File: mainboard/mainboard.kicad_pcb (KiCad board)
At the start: 2 copper layers, 103 x 41 mm, 25 parts, among them P1 CONN_01X06, P2 CONN_01X08, P3 CONN_01X08, SW1 SW_PUSH, SW2 SW_PUSH, SW3 SW_PUSH, SW4 SW_PUSH, SW5 SW_PUSH, SW6 SW_PUSH, U1 LPC812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

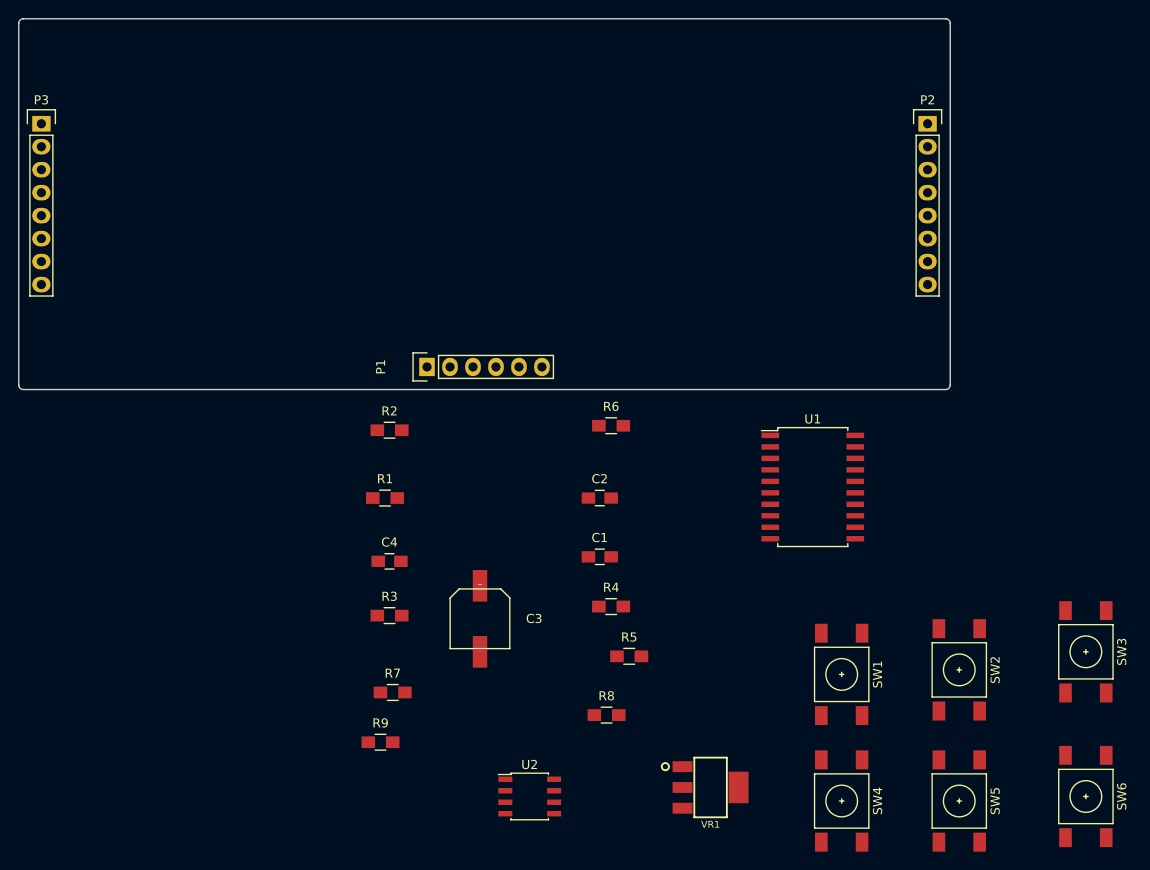
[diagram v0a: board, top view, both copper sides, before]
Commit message: Component placement on PCB.
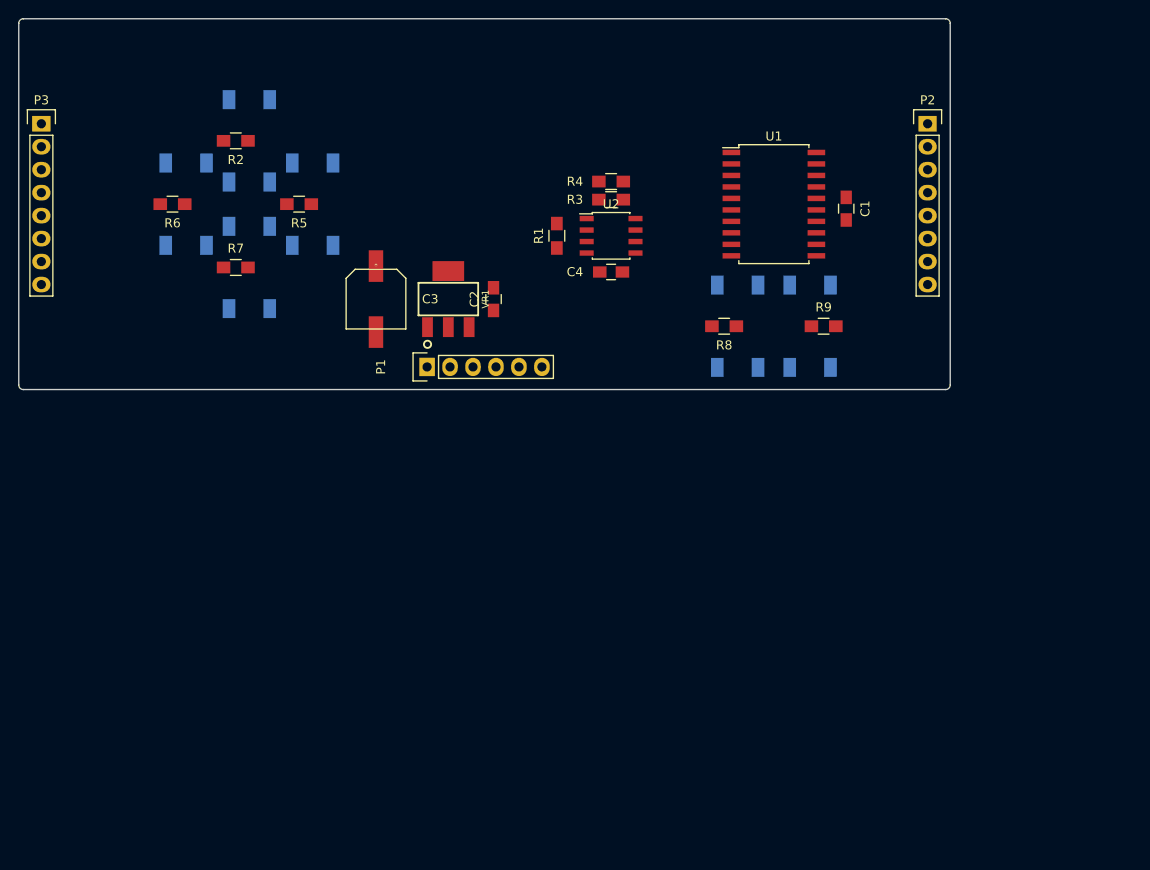
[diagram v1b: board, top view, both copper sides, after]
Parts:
- SW1, SW2, SW3, SW4, SW5, SW6: moved to B.Cu
- moved SW3 111.1 mm to (-33.0, 0.00)
- moved SW2 90.2 mm to (-26.0, 7.00)
- moved SW4 88.2 mm to (-19.0, 0.00)
- moved SW1 88.2 mm to (-26.0, -7.00)
- moved R9 67.2 mm to (37.5, 13.5)
- moved U2 62.6 mm to (14.0, 3.50)
- moved R5 61.9 mm to (-20.5, 0.00), turned to 180 degrees
- moved VR1 61.3 mm to (-4.00, 10.5), turned to 90 degrees
- moved SW6 60.3 mm to (36.0, 13.5), turned to 180 degrees
- moved SW5 57.9 mm to (28.0, 13.5)
- moved R6 54.3 mm to (-34.5, 0.00), turned to 180 degrees
- moved R3 52.1 mm to (14.0, -0.50)
- moved R7 50.1 mm to (-27.5, 7.00)
- moved C1 47.2 mm to (40.0, 0.50), turned to 270 degrees
- moved R4 47.0 mm to (14.0, -2.50)
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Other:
- board text added: "Mini Clock v0.1 By Martin Atkins https://github.com/apparentlymart/miniclock"

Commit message: DC regulator traces.
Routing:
- net GND: track 0.00 -> 19.7 mm
- net +5V: track 0.00 -> 8.72 mm
- net +3V3: track 0.00 -> 8.23 mm
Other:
- net class Default: trace_width 0.25 -> 0.2
- net class Power added: clearance 0.2, trace_width 0.4, via_dia 0.8, via_drill 0.4
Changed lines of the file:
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@@
     (thickness 1.6)
     (drawings 9)
-    (tracks 0)
+    (tracks 15)
     (zones 0)
     (modules 25)
@@
   )
   (setup
-    (last_trace_width 0.25)
+    (last_trace_width 0.2)
     (trace_clearance 0.2)
     (zone_clearance 0.508)
@@
   (net_class Default "This is the default net class."
     (clearance 0.2)
-    (trace_width 0.25)
+    (trace_width 0.2)
     (via_dia 0.6)
     (via_drill 0.4)
     (uvia_dia 0.3)
     (uvia_drill 0.1)
-    (add_net +3V3)
-    (add_net +5V)
     (add_net CTS)
-    (add_net GND)
     (add_net MISO)
     (add_net MOSI)
@@
     (add_net ~RIGHT)
     (add_net ~UP)
+  )
+  (net_class Power ""
+    (clearance 0.2)
+    (trace_width 0.4)
+    (via_dia 0.8)
+    (via_drill 0.4)
+    (uvia_dia 0.3)
+    (uvia_drill 0.1)
+    (add_net +3V3)
+    (add_net +5V)
+    (add_net GND)
   )
   (module Capacitors_SMD:C_0805_HandSoldering (layer F.Cu)
@@
   (gr_line (start -51 20.5) (end 51 20.5) (layer Edge.Cuts) (width 0.15))
   (gr_line (start -51.5 -20) (end -51.5 20) (layer Edge.Cuts) (width 0.15))
+  (segment (start -12 14.15) (end -6.85 14.15) (width 0.4) (layer F.Cu) (net 1))
+  (segment (start -6.85 14.15) (end -6.3 13.6) (width 0.4) (layer F.Cu) (net 1))
+  (segment (start 1 9.25) (end -2.45 9.25) (width 0.4) (layer F.Cu) (net 1))
+  (segment (start -2.45 9.25) (end -6.3 13.1) (width 0.4) (layer F.Cu) (net 1))
+  (segment (start -6.3 13.1) (end -6.3 13.6) (width 0.4) (layer F.Cu) (net 1))
+  (segment (start -6.35 18) (end -6.35 13.65) (width 0.4) (layer F.Cu) (net 1))
+  (segment (start -6.35 13.65) (end -6.3 13.6) (width 0.4) (layer F.Cu) (net 1))
+  (segment (start -12 6.85) (end -4.55 6.85) (width 0.4) (layer F.Cu) (net 2))
+  (segment (start -4.55 6.85) (end -4 7.4) (width 0.4) (layer F.Cu) (net 2))
+  (segment (start 1 11.75) (end 1 12.9) (width 0.4) (layer F.Cu) (net 3))
+  (segment (start 1 12.9) (end 0.3 13.6) (width 0.4) (layer F.Cu) (net 3))
+  (segment (start 0.3 13.6) (end -0.7 13.6) (width 0.4) (layer F.Cu) (net 3))
+  (segment (start -0.7 13.6) (end -1.7 13.6) (width 0.4) (layer F.Cu) (net 3))
+  (segment (start -1.7 13.6) (end -1.7 17.57) (width 0.4) (layer F.Cu) (net 3))
+  (segment (start -1.7 17.57) (end -1.27 18) (width 0.4) (layer F.Cu) (net 3))
 )

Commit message: Button traces.
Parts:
- moved R5 9.90 mm to (-27.5, 7.00)
- moved R7 9.90 mm to (-20.5, 0.00), turned to 180 degrees
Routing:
- net Net-(R9-Pad2): track 0.00 -> 11.1 mm, vias 0 -> 1
- net Net-(R8-Pad2): track 0.00 -> 11.1 mm, vias 0 -> 1
- net Net-(R2-Pad2): track 0.00 -> 11.1 mm, vias 0 -> 1
- net Net-(R7-Pad2): track 0.00 -> 11.1 mm, vias 0 -> 1
- net Net-(R6-Pad2): track 0.00 -> 11.1 mm, vias 0 -> 1
- net Net-(R5-Pad2): track 0.00 -> 11.1 mm, vias 0 -> 1
- net GND: track 19.7 -> 29.6 mm, vias 0 -> 6
- added copper zone on B.Cu, net GND
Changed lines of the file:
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@@
     (thickness 1.6)
     (drawings 9)
-    (tracks 15)
+    (tracks 63)
     (zones 0)
     (modules 25)
@@
   )
   (module Resistors_SMD:R_0805_HandSoldering (layer F.Cu)
-    (at -20.5 0 180)
+    (at -27.5 7 180)
     (descr "Resistor SMD 0805, hand soldering")
     (tags "resistor 0805")
@@
   )
   (module Resistors_SMD:R_0805_HandSoldering (layer F.Cu)
-    (at -27.5 7)
+    (at -20.5 0 180)
     (descr "Resistor SMD 0805, hand soldering")
     (tags "resistor 0805")
     (attr smd)
-    (fp_text reference R7 (at 0 -2.1) (layer F.SilkS)
-      (effects (font (size 1 1) (thickness 0.15)))
-    )
-    (fp_text value R (at 0 2.1) (layer F.Fab)
+    (fp_text reference R7 (at 0 -2.1 180) (layer F.SilkS)
+      (effects (font (size 1 1) (thickness 0.15)))
+    )
+    (fp_text value R (at 0 2.1 180) (layer F.Fab)
       (effects (font (size 1 1) (thickness 0.15)))
     )
@@
     (fp_line (start 0.6 0.875) (end -0.6 0.875) (layer F.SilkS) (width 0.15))
     (fp_line (start -0.6 -0.875) (end 0.6 -0.875) (layer F.SilkS) (width 0.15))
-    (pad 1 smd rect (at -1.35 0) (size 1.5 1.3) (layers F.Cu F.Paste F.Mask)
-      (net 1 GND))
-    (pad 2 smd rect (at 1.35 0) (size 1.5 1.3) (layers F.Cu F.Paste F.Mask)
+    (pad 1 smd rect (at -1.35 0 180) (size 1.5 1.3) (layers F.Cu F.Paste F.Mask)
+      (net 1 GND))
+    (pad 2 smd rect (at 1.35 0 180) (size 1.5 1.3) (layers F.Cu F.Paste F.Mask)
       (net 27 "Net-(R7-Pad2)"))
     (model Resistors_SMD.3dshapes/R_0805_HandSoldering.wrl
@@
   (gr_line (start -51 20.5) (end 51 20.5) (layer Edge.Cuts) (width 0.15))
   (gr_line (start -51.5 -20) (end -51.5 20) (layer Edge.Cuts) (width 0.15))
+  (segment (start 36.15 13.5) (end 34.5 13.5) (width 0.4) (layer F.Cu) (net 1))
+  (via (at 34.5 13.5) (size 0.8) (drill 0.4) (layers F.Cu B.Cu) (net 1))
+  (segment (start 27.85 13.5) (end 29.5 13.5) (width 0.4) (layer F.Cu) (net 1))
+  (via (at 29.5 13.5) (size 0.8) (drill 0.4) (layers F.Cu B.Cu) (net 1))
+  (segment (start -26.15 7) (end -24.5 7) (width 0.4) (layer F.Cu) (net 1))
+  (via (at -24.5 7) (size 0.8) (drill 0.4) (layers F.Cu B.Cu) (net 1))
+  (segment (start -26.15 -7) (end -24.5 -7) (width 0.4) (layer F.Cu) (net 1))
+  (via (at -24.5 -7) (size 0.8) (drill 0.4) (layers F.Cu B.Cu) (net 1))
+  (segment (start -33.15 0) (end -31.5 0) (width 0.4) (layer F.Cu) (net 1))
+  (via (at -31.5 0) (size 0.8) (drill 0.4) (layers F.Cu B.Cu) (net 1))
+  (segment (start -19.15 0) (end -17.5 0) (width 0.4) (layer F.Cu) (net 1))
+  (via (at -17.5 0) (size 0.8) (drill 0.4) (layers F.Cu B.Cu) (net 1))
   (segment (start -12 14.15) (end -6.85 14.15) (width 0.4) (layer F.Cu) (net 1))
   (segment (start -6.85 14.15) (end -6.3 13.6) (width 0.4) (layer F.Cu) (net 1))
@@
   (segment (start -1.7 13.6) (end -1.7 17.57) (width 0.4) (layer F.Cu) (net 3))
   (segment (start -1.7 17.57) (end -1.27 18) (width 0.4) (layer F.Cu) (net 3))
+  (segment (start -27.5 -7) (end -27.5 -3.2) (width 0.2) (layer B.Cu) (net 22))
+  (segment (start -27.5 -3.2) (end -28.25 -2.45) (width 0.2) (layer B.Cu) (net 22))
+  (segment (start -27.5 -7) (end -27.5 -10.8) (width 0.2) (layer B.Cu) (net 22))
+  (segment (start -27.5 -10.8) (end -28.25 -11.55) (width 0.2) (layer B.Cu) (net 22))
+  (segment (start -28.85 -7) (end -27.5 -7) (width 0.2) (layer F.Cu) (net 22))
+  (via (at -27.5 -7) (size 0.6) (drill 0.4) (layers F.Cu B.Cu) (net 22))
+  (segment (start -27.5 7) (end -27.5 10.8) (width 0.2) (layer B.Cu) (net 25))
+  (segment (start -27.5 10.8) (end -28.25 11.55) (width 0.2) (layer B.Cu) (net 25))
+  (segment (start -27.5 7) (end -27.5 3.2) (width 0.2) (layer B.Cu) (net 25))
+  (segment (start -27.5 3.2) (end -28.25 2.45) (width 0.2) (layer B.Cu) (net 25))
+  (segment (start -28.85 7) (end -27.5 7) (width 0.2) (layer F.Cu) (net 25))
+  (via (at -27.5 7) (size 0.6) (drill 0.4) (layers F.Cu B.Cu) (net 25))
+  (segment (start -34.5 0) (end -34.5 3.8) (width 0.2) (layer B.Cu) (net 26))
+  (segment (start -34.5 3.8) (end -35.25 4.55) (width 0.2) (layer B.Cu) (net 26))
+  (segment (start -34.5 0) (end -34.5 -3.8) (width 0.2) (layer B.Cu) (net 26))
+  (segment (start -34.5 -3.8) (end -35.25 -4.55) (width 0.2) (layer B.Cu) (net 26))
+  (segment (start -35.85 0) (end -34.5 0) (width 0.2) (layer F.Cu) (net 26))
+  (via (at -34.5 0) (size 0.6) (drill 0.4) (layers F.Cu B.Cu) (net 26))
+  (segment (start -20.5 0) (end -20.5 3.8) (width 0.2) (layer B.Cu) (net 27))
+  (segment (start -20.5 3.8) (end -21.25 4.55) (width 0.2) (layer B.Cu) (net 27))
+  (segment (start -20.5 0) (end -20.5 -3.8) (width 0.2) (layer B.Cu) (net 27))
+  (segment (start -20.5 -3.8) (end -21.25 -4.55) (width 0.2) (layer B.Cu) (net 27))
+  (segment (start -21.85 0) (end -20.5 0) (width 0.2) (layer F.Cu) (net 27))
+  (via (at -20.5 0) (size 0.6) (drill 0.4) (layers F.Cu B.Cu) (net 27))
+  (segment (start 26.5 13.5) (end 26.5 17.3) (width 0.2) (layer B.Cu) (net 28))
+  (segment (start 26.5 17.3) (end 25.75 18.05) (width 0.2) (layer B.Cu) (net 28))
+  (segment (start 26.5 13.5) (end 26.5 9.7) (width 0.2) (layer B.Cu) (net 28))
+  (segment (start 26.5 9.7) (end 25.75 8.95) (width 0.2) (layer B.Cu) (net 28))
+  (segment (start 25.15 13.5) (end 26.5 13.5) (width 0.2) (layer F.Cu) (net 28))
+  (via (at 26.5 13.5) (size 0.6) (drill 0.4) (layers F.Cu B.Cu) (net 28))
+  (segment (start 37.5 13.5) (end 37.5 17.3) (width 0.2) (layer B.Cu) (net 29))
+  (segment (start 37.5 17.3) (end 38.25 18.05) (width 0.2) (layer B.Cu) (net 29))
+  (segment (start 37.5 13.5) (end 37.5 9.7) (width 0.2) (layer B.Cu) (net 29))
+  (segment (start 37.5 9.7) (end 38.25 8.95) (width 0.2) (layer B.Cu) (net 29))
+  (segment (start 38.85 13.5) (end 37.5 13.5) (width 0.2) (layer F.Cu) (net 29))
+  (via (at 37.5 13.5) (size 0.6) (drill 0.4) (layers F.Cu B.Cu) (net 29))
+  (zone (net 1) (net_name GND) (layer B.Cu) (hatch edge 0.508)
+    (connect_pads (clearance 0.508))
+    (min_thickness 0.254)
+    (fill yes (arc_segments 16) (thermal_gap 0.508) (thermal_bridge_width 0.508))
+    (polygon
+      (pts
+        (xy -51 -20) (xy 51 -20) (xy 51 20) (xy -51 20)
+      )
+    )
+  )
 )

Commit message: RTC traces.
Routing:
- net +3V3: track 8.23 -> 23.2 mm
- net SDA: track 0.00 -> 7.15 mm
- net GND: track 29.6 -> 33.6 mm
- net SQW: track 0.00 -> 3.60 mm
- net SCL: track 0.00 -> 2.71 mm
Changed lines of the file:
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@@
     (thickness 1.6)
     (drawings 9)
-    (tracks 63)
+    (tracks 84)
     (zones 0)
     (modules 25)
@@
   (gr_line (start -51 20.5) (end 51 20.5) (layer Edge.Cuts) (width 0.15))
   (gr_line (start -51.5 -20) (end -51.5 20) (layer Edge.Cuts) (width 0.15))
+  (segment (start 16.7 4.135) (end 16.7 5.405) (width 0.4) (layer F.Cu) (net 1))
+  (segment (start 16.7 5.405) (end 16.7 6.05) (width 0.4) (layer F.Cu) (net 1))
+  (segment (start 16.7 6.05) (end 15.25 7.5) (width 0.4) (layer F.Cu) (net 1))
   (segment (start 36.15 13.5) (end 34.5 13.5) (width 0.4) (layer F.Cu) (net 1))
   (via (at 34.5 13.5) (size 0.8) (drill 0.4) (layers F.Cu B.Cu) (net 1))
@@
   (segment (start -6.35 18) (end -6.35 13.65) (width 0.4) (layer F.Cu) (net 1))
   (segment (start -6.35 13.65) (end -6.3 13.6) (width 0.4) (layer F.Cu) (net 1))
+  (segment (start 12.75 7.5) (end 12.75 3.14) (width 0.4) (layer F.Cu) (net 2))
+  (segment (start 12.75 3.14) (end 12.475 2.865) (width 0.4) (layer F.Cu) (net 2))
+  (segment (start 12.475 2.865) (end 11.3 2.865) (width 0.4) (layer F.Cu) (net 2))
+  (segment (start 12.65 -2.5) (end 12.65 -0.5) (width 0.4) (layer F.Cu) (net 2))
+  (segment (start 12.65 -0.5) (end 12.65 2.69) (width 0.4) (layer F.Cu) (net 2))
+  (segment (start 12.65 2.69) (end 12.475 2.865) (width 0.4) (layer F.Cu) (net 2))
+  (segment (start 11.3 2.865) (end 8.715 2.865) (width 0.4) (layer F.Cu) (net 2))
+  (segment (start 8.715 2.865) (end 8 2.15) (width 0.4) (layer F.Cu) (net 2))
   (segment (start -12 6.85) (end -4.55 6.85) (width 0.4) (layer F.Cu) (net 2))
   (segment (start -4.55 6.85) (end -4 7.4) (width 0.4) (layer F.Cu) (net 2))
@@
   (segment (start -1.7 13.6) (end -1.7 17.57) (width 0.4) (layer F.Cu) (net 3))
   (segment (start -1.7 17.57) (end -1.27 18) (width 0.4) (layer F.Cu) (net 3))
+  (segment (start 11.3 4.135) (end 8.715 4.135) (width 0.2) (layer F.Cu) (net 21))
+  (segment (start 8.715 4.135) (end 8 4.85) (width 0.2) (layer F.Cu) (net 21))
   (segment (start -27.5 -7) (end -27.5 -3.2) (width 0.2) (layer B.Cu) (net 22))
   (segment (start -27.5 -3.2) (end -28.25 -2.45) (width 0.2) (layer B.Cu) (net 22))
@@
   (segment (start -28.85 -7) (end -27.5 -7) (width 0.2) (layer F.Cu) (net 22))
   (via (at -27.5 -7) (size 0.6) (drill 0.4) (layers F.Cu B.Cu) (net 22))
+  (segment (start 16.7 1.595) (end 16.7 0.75) (width 0.2) (layer F.Cu) (net 23))
+  (segment (start 16.7 0.75) (end 15.45 -0.5) (width 0.2) (layer F.Cu) (net 23))
+  (segment (start 15.45 -0.5) (end 15.35 -0.5) (width 0.2) (layer F.Cu) (net 23))
+  (segment (start 16.7 2.865) (end 17.175 2.865) (width 0.2) (layer F.Cu) (net 24))
+  (segment (start 17.775001 2.264999) (end 17.775001 -0.174999) (width 0.2) (layer F.Cu) (net 24))
+  (segment (start 17.175 2.865) (end 17.775001 2.264999) (width 0.2) (layer F.Cu) (net 24))
+  (segment (start 17.775001 -0.174999) (end 15.45 -2.5) (width 0.2) (layer F.Cu) (net 24))
+  (segment (start 15.45 -2.5) (end 15.35 -2.5) (width 0.2) (layer F.Cu) (net 24))
   (segment (start -27.5 7) (end -27.5 10.8) (width 0.2) (layer B.Cu) (net 25))
   (segment (start -27.5 10.8) (end -28.25 11.55) (width 0.2) (layer B.Cu) (net 25))

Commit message: Remaining traces.
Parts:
- added REF**: STRAINHOLE, miniclock:STRAINHOLE, F.Cu at (-9.50, 18.0)
- added REF**: STRAINHOLE, miniclock:STRAINHOLE, F.Cu at (9.50, 18.0)
- moved C1 0.50 mm to (40.0, 0.00)
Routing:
- net ~RESET: track 0.00 -> 73.7 mm, vias 0 -> 5
- net ~LEFT: track 0.00 -> 71.7 mm, vias 0 -> 3
- net ~DOWN: track 0.00 -> 63.1 mm, vias 0 -> 3
- net ~UP: track 0.00 -> 62.7 mm, vias 0 -> 1
- net ~RIGHT: track 0.00 -> 57.0 mm, vias 0 -> 1
- net RXD: track 0.00 -> 53.1 mm
- net TXD: track 0.00 -> 41.5 mm
- net ~ISP: track 0.00 -> 25.0 mm, vias 0 -> 1
- net SQW: track 3.60 -> 22.0 mm, vias 0 -> 2
- net SDA: track 7.15 -> 22.1 mm, vias 0 -> 2
- net SCL: track 2.71 -> 17.4 mm, vias 0 -> 2
- net SSEL: track 0.00 -> 13.7 mm
- net MISO: track 0.00 -> 13.2 mm
- net SCLK: track 0.00 -> 12.9 mm
- net MOSI: track 0.00 -> 12.6 mm
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- added copper zone on F.Cu, net +3V3
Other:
- board text added: "Mini Clock: Main Board v0.1 By Martin Atkins https://github.com/apparentlymart/miniclock"
- board text removed: "Mini Clock v0.1 By Martin Atkins https://github.com/apparentlymart/miniclock"

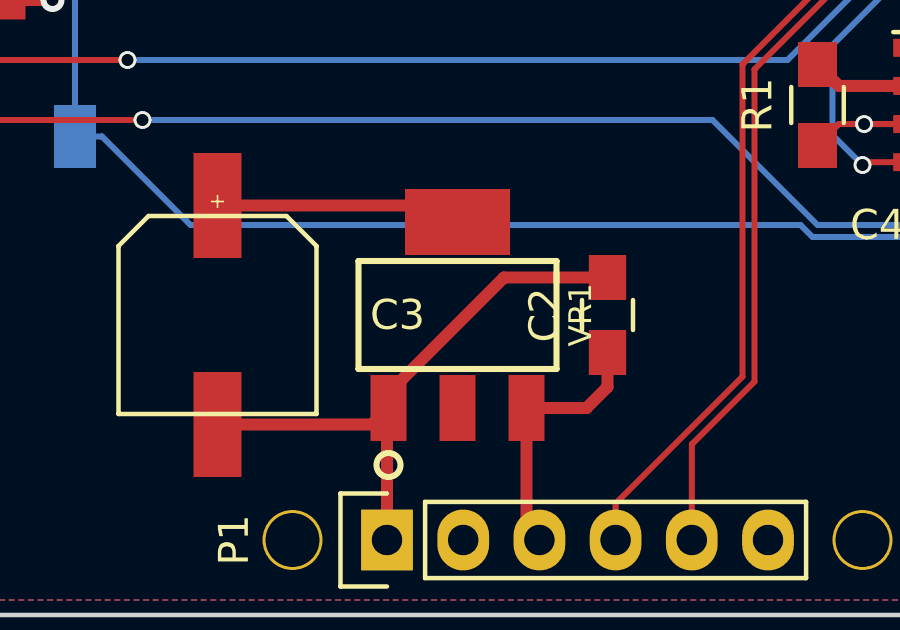
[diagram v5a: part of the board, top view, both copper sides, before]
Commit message: Connect final missing link.
(This isn't actually really needed since these things are connected
internally within the regulator, but this pacifies the KiCad DRC.
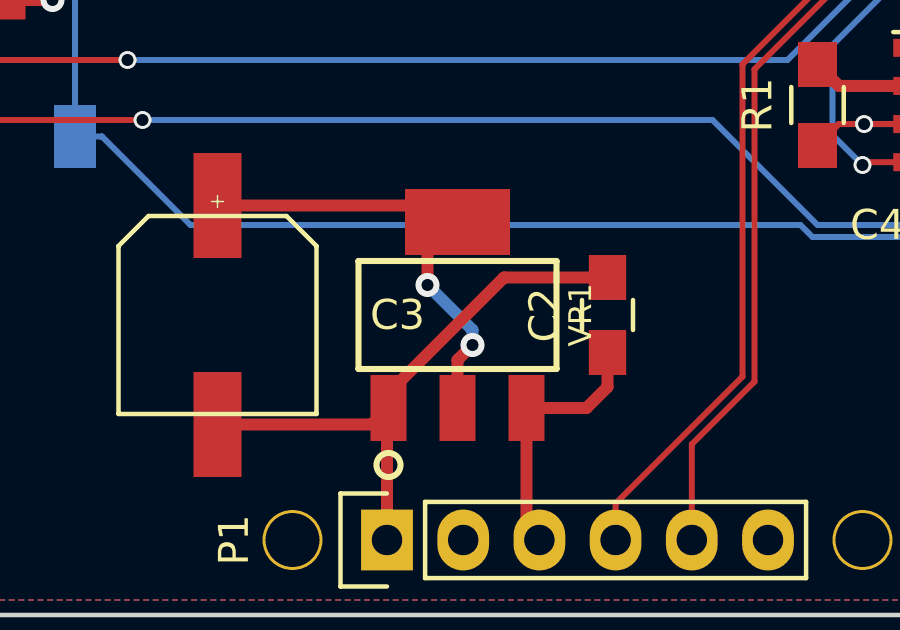
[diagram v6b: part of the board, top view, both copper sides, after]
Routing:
- net +3V3: track 26.7 -> 34.2 mm, vias 0 -> 2
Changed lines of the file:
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@@
 (kicad_pcb (version 4) (host pcbnew 0.201509051501+6156~29~ubuntu15.04.1-product)
   (general
-    (links 0)
-    (no_connects 55)
+    (links 66)
+    (no_connects 1)
     (area -51.575001 -20.575001 51.575001 20.575001)
     (thickness 1.6)
     (drawings 9)
-    (tracks 230)
+    (tracks 238)
     (zones 0)
     (modules 27)
@@
   (segment (start -6.35 18) (end -6.35 13.65) (width 0.4) (layer F.Cu) (net 1))
   (segment (start -6.35 13.65) (end -6.3 13.6) (width 0.4) (layer F.Cu) (net 1))
+  (segment (start -5 9.5) (end -5 8.4) (width 0.4) (layer F.Cu) (net 2))
+  (segment (start -5 8.4) (end -4 7.4) (width 0.4) (layer F.Cu) (net 2))
+  (segment (start -3.5 11.5) (end -3.5 11) (width 0.4) (layer B.Cu) (net 2))
+  (segment (start -3.5 11) (end -5 9.5) (width 0.4) (layer B.Cu) (net 2))
+  (via (at -5 9.5) (size 0.8) (drill 0.4) (layers F.Cu B.Cu) (net 2))
+  (segment (start -4 13.6) (end -4 12) (width 0.4) (layer F.Cu) (net 2))
+  (segment (start -4 12) (end -3.5 11.5) (width 0.4) (layer F.Cu) (net 2))
+  (via (at -3.5 11.5) (size 0.8) (drill 0.4) (layers F.Cu B.Cu) (net 2))
   (segment (start 36.7 0.635) (end 39.385 0.635) (width 0.4) (layer F.Cu) (net 2))
   (segment (start 39.385 0.635) (end 40 1.25) (width 0.4) (layer F.Cu) (net 2))
